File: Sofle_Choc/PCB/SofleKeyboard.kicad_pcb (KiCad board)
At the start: 2 copper layers, 179.3 x 122 mm, 94 parts, among them J2 4PIN, J3 OLED, P1 i2c_pin, P2 i2c_pin, SW1 SW_PUSH_LED, SW10 SW_PUSH_LED, SW11 SW_PUSH_LED, SW12 SW_PUSH_LED, SW13 SW_PUSH_LED, SW14 SW_PUSH_LED, SW15 SW_PUSH_LED, SW16 SW_PUSH_LED, SW17 SW_PUSH_LED, SW18 SW_PUSH_LED, SW19 SW_PUSH_LED, SW2 SW_PUSH_LED, SW20 SW_PUSH_LED, SW21 SW_PUSH_LED, SW22 SW_PUSH_LED, SW23 SW_PUSH_LED, SW24 SW_PUSH_LED, SW25 Rotary_Encoder_Switch, SW26 SW_PUSH_LED, SW27 SW_PUSH_LED, SW28 SW_PUSH_LED, SW29 SW_PUSH_LED, SW3 SW_PUSH_LED, SW30 SW_PUSH_LED, SW31 SW_PUSH_LED, SW32 SW_PUSH_LED, SW33 SW_PUSH_LED, SW34 SW_PUSH_LED, SW35 SW_PUSH_LED, SW4 SW_PUSH_LED, SW5 SW_PUSH_LED, SW6 SW_PUSH_LED, SW7 SW_PUSH_LED, SW8 SW_PUSH_LED, SW9 SW_PUSH_LED, U1 ProMicro

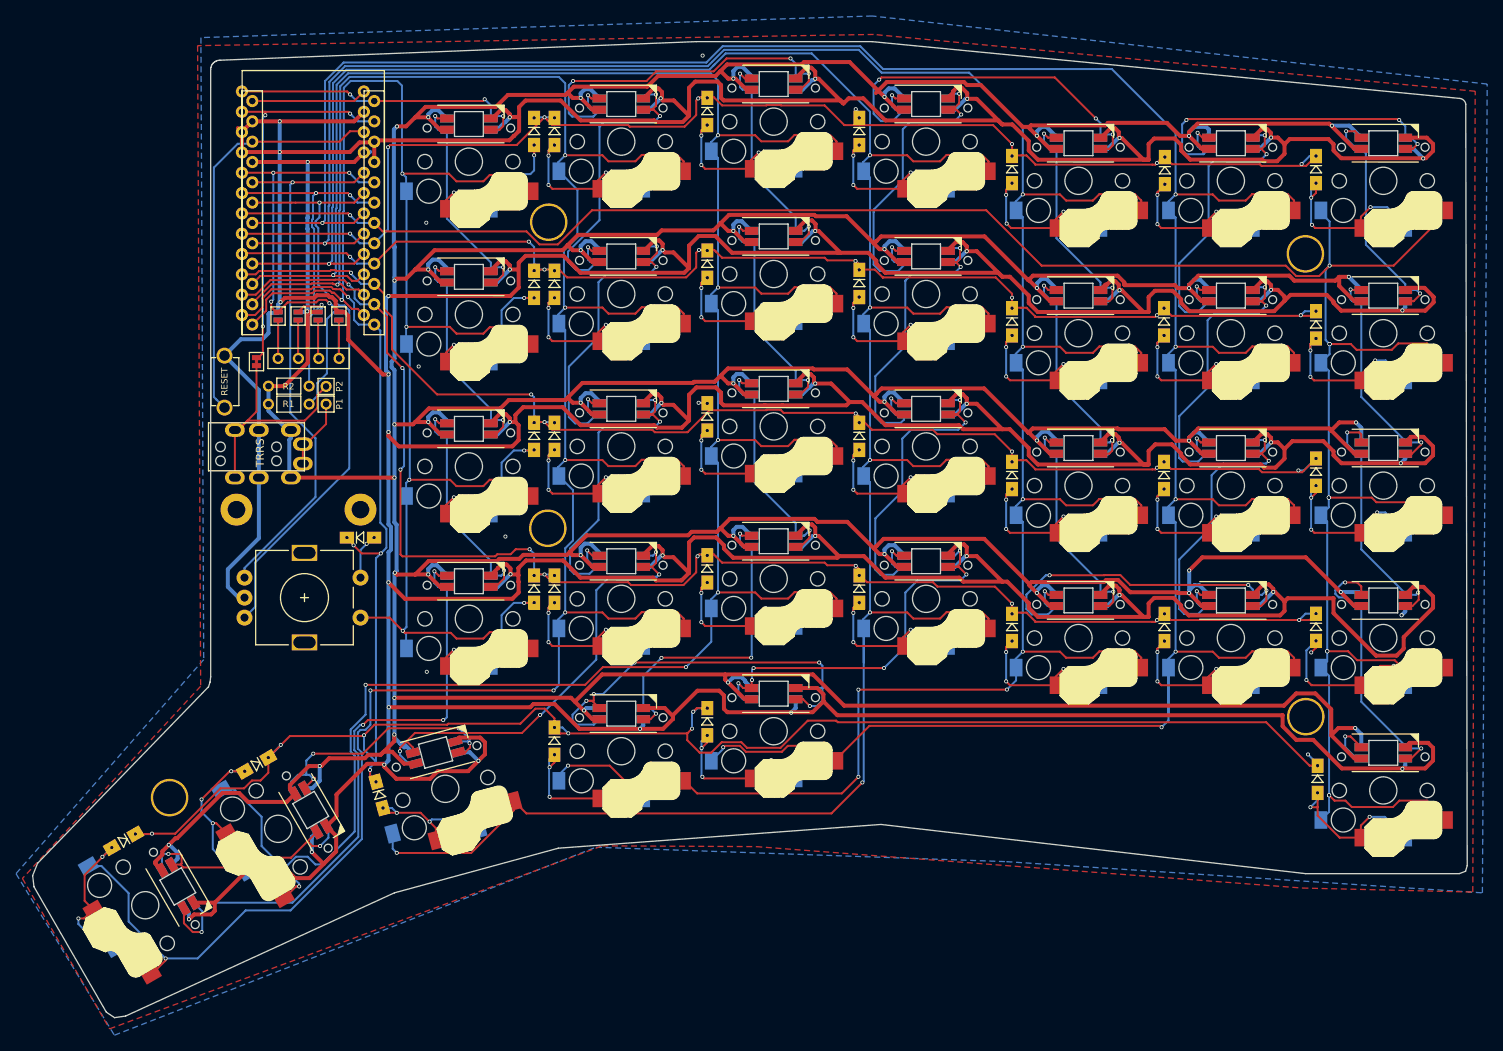
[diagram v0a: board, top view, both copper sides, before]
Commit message: Make smooth edge cut corners
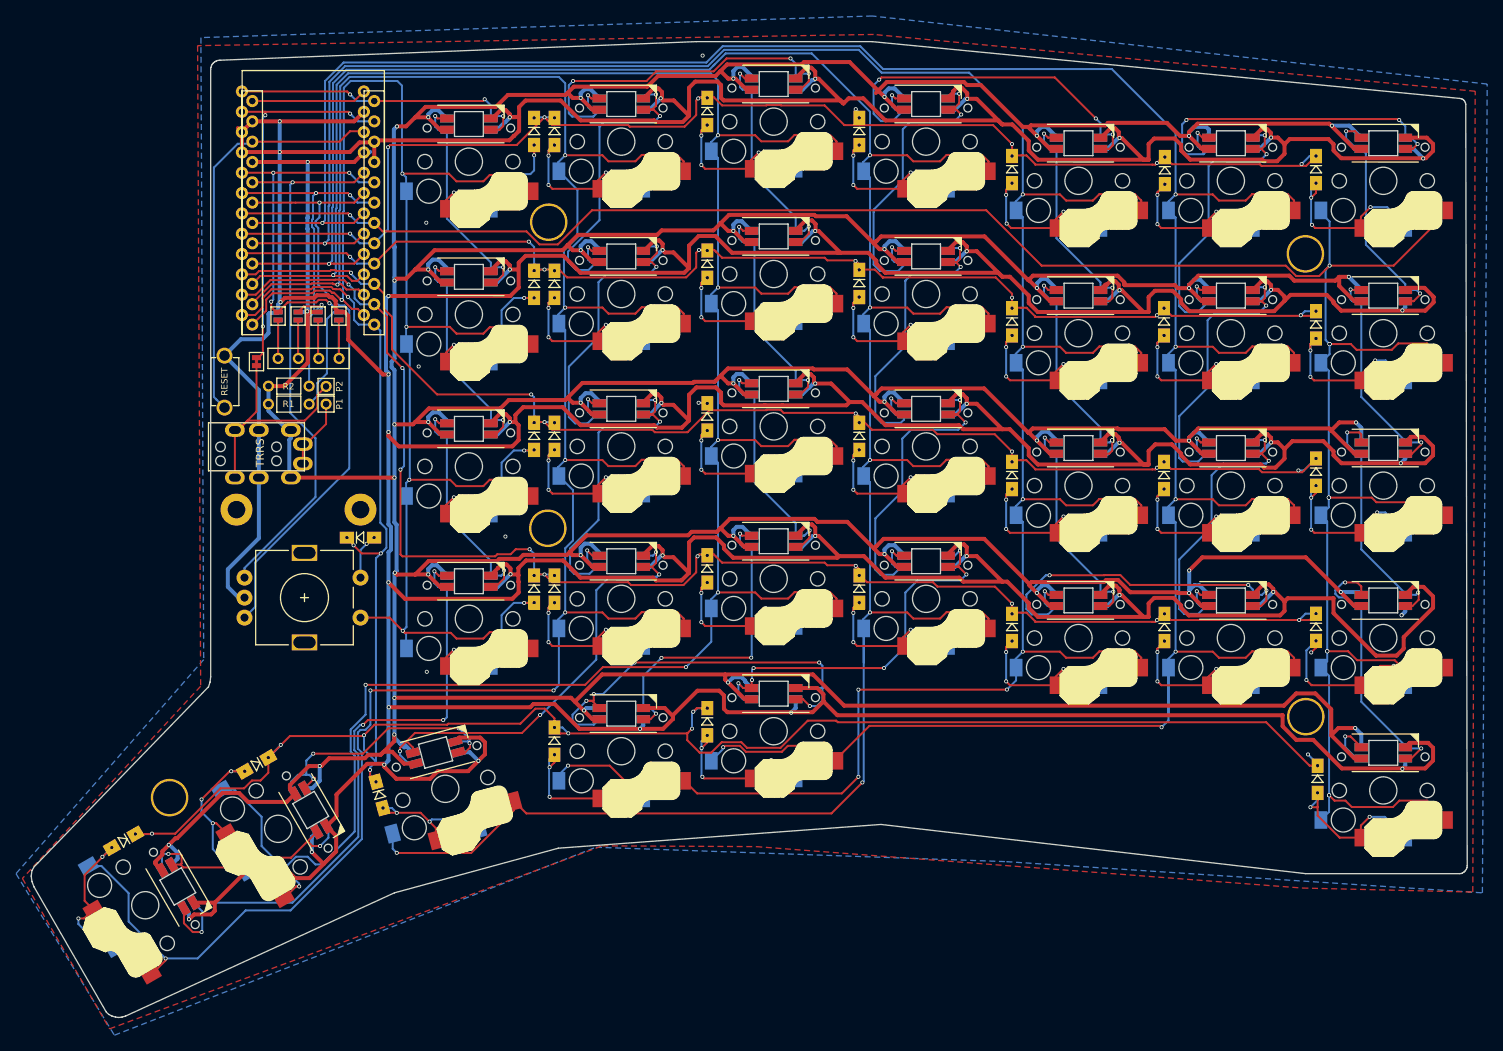
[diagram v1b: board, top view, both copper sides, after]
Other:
- board size 179.3 x 122 mm -> 179.5 x 122 mm
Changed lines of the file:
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@@
   (gr_line (start 131.72912 135.82264) (end 111.23912 141.40264)
     (stroke (width 0.1) (type solid)) (layer "Edge.Cuts"))
-  (gr_arc (start 244.395788 42.098905) (mid 244.903099 42.328253) (end 245.159119 42.82264)
+  (gr_line (start 225.13912 139.00264) (end 244.33912 139.00264)
     (stroke (width 0.15) (type default)) (layer "Edge.Cuts"))
-  (gr_line (start 245.13912 138.70264) (end 245.33912 138.00264)
+  (gr_line (start 65.93912 138.60264) (end 66.23912 138.10264)
     (stroke (width 0.15) (type default)) (layer "Edge.Cuts"))
-  (gr_line (start 225.13912 139.00264) (end 244.33912 139.00264)
+  (gr_line (start 245.15912 42.82264) (end 245.10912 42.63264)
+    (stroke (width 0.15) (type default)) (layer "Edge.Cuts"))
+  (gr_line (start 245.30912 138.25264) (end 245.22912 138.46264)
+    (stroke (width 0.15) (type default)) (layer "Edge.Cuts"))
+  (gr_line (start 245.33912 138.00264) (end 245.30912 138.25264)
+    (stroke (width 0.15) (type default)) (layer "Edge.Cuts"))
+  (gr_line (start 65.83912 139.30264) (end 65.93912 138.60264)
     (stroke (width 0.15) (type default)) (layer "Edge.Cuts"))
   (gr_line (start 66.18912 140.65264) (end 75.22912 156.31264)
     (stroke (width 0.15) (type default)) (layer "Edge.Cuts"))
-  (gr_line (start 66.63912 137.70264) (end 66.01912 139.25264)
+  (gr_line (start 76.77912 156.98264) (end 76.37912 156.93264)
     (stroke (width 0.15) (type default)) (layer "Edge.Cuts"))
   (gr_line (start 245.33912 138.00264) (end 245.15912 42.82264)
     (stroke (width 0.15) (type default)) (layer "Edge.Cuts"))
-  (gr_line (start 66.01912 139.25264) (end 66.18912 140.65264)
+  (gr_line (start 244.73912 138.92264) (end 244.55912 138.99264)
     (stroke (width 0.15) (type default)) (layer "Edge.Cuts"))
-  (gr_line (start 76.25912 157.00264) (end 75.22912 156.31264)
-    (stroke (width 0.15) (type default)) (layer "Edge.Cuts"))
-  (gr_line (start 76.25912 157.00264) (end 77.63912 156.80264)
+  (gr_line (start 244.55912 138.99264) (end 244.33912 139.00264)
     (stroke (width 0.15) (type default)) (layer "Edge.Cuts"))
   (gr_line (start 172.05912 132.85264) (end 225.13912 139.00264)
     (stroke (width 0.15) (type default)) (layer "Edge.Cuts"))
-  (gr_line (start 244.33912 139.00264) (end 245.13912 138.70264)
+  (gr_line (start 76.37912 156.93264) (end 75.93912 156.80264)
+    (stroke (width 0.15) (type default)) (layer "Edge.Cuts"))
+  (gr_line (start 244.92912 138.81264) (end 244.73912 138.92264)
+    (stroke (width 0.15) (type default)) (layer "Edge.Cuts"))
+  (gr_line (start 75.22912 156.31264) (end 75.53912 156.60264)
+    (stroke (width 0.15) (type default)) (layer "Edge.Cuts"))
+  (gr_line (start 244.61912 42.14264) (end 244.395788 42.098905)
+    (stroke (width 0.15) (type default)) (layer "Edge.Cuts"))
+  (gr_line (start 244.76912 42.20264) (end 244.61912 42.14264)
+    (stroke (width 0.15) (type default)) (layer "Edge.Cuts"))
+  (gr_line (start 66.18912 140.65264) (end 65.93912 140.00264)
+    (stroke (width 0.15) (type default)) (layer "Edge.Cuts"))
+  (gr_line (start 245.10912 42.63264) (end 245.01912 42.44264)
+    (stroke (width 0.15) (type default)) (layer "Edge.Cuts"))
+  (gr_line (start 77.63912 156.80264) (end 77.18912 156.93264)
+    (stroke (width 0.15) (type default)) (layer "Edge.Cuts"))
+  (gr_line (start 245.22912 138.46264) (end 245.09912 138.64264)
+    (stroke (width 0.15) (type default)) (layer "Edge.Cuts"))
+  (gr_line (start 66.23912 138.10264) (end 66.63912 137.70264)
+    (stroke (width 0.15) (type default)) (layer "Edge.Cuts"))
+  (gr_line (start 245.01912 42.44264) (end 244.89912 42.30264)
+    (stroke (width 0.15) (type default)) (layer "Edge.Cuts"))
+  (gr_line (start 245.09912 138.64264) (end 244.92912 138.81264)
+    (stroke (width 0.15) (type default)) (layer "Edge.Cuts"))
+  (gr_line (start 77.18912 156.93264) (end 76.77912 156.98264)
+    (stroke (width 0.15) (type default)) (layer "Edge.Cuts"))
+  (gr_line (start 65.93912 140.00264) (end 65.83912 139.30264)
     (stroke (width 0.15) (type default)) (layer "Edge.Cuts"))
   (gr_line (start 77.63912 156.80264) (end 111.23912 141.40264)
     (stroke (width 0.15) (type default)) (layer "Edge.Cuts"))
+  (gr_line (start 244.89912 42.30264) (end 244.76912 42.20264)
+    (stroke (width 0.15) (type default)) (layer "Edge.Cuts"))
+  (gr_line (start 75.53912 156.60264) (end 75.93912 156.80264)
+    (stroke (width 0.15) (type default)) (layer "Edge.Cuts"))
   (gr_text "s16" (at 177.5 80.81464) (layer "Eco1.User")
